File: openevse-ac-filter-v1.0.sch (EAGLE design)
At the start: 8 parts

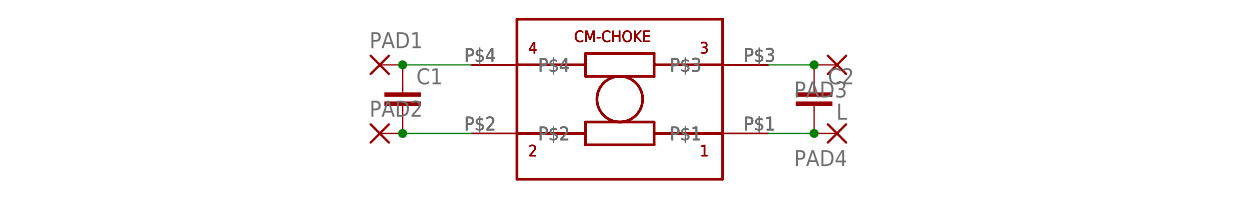
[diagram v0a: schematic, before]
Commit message: V1.2 increase pad and hole size
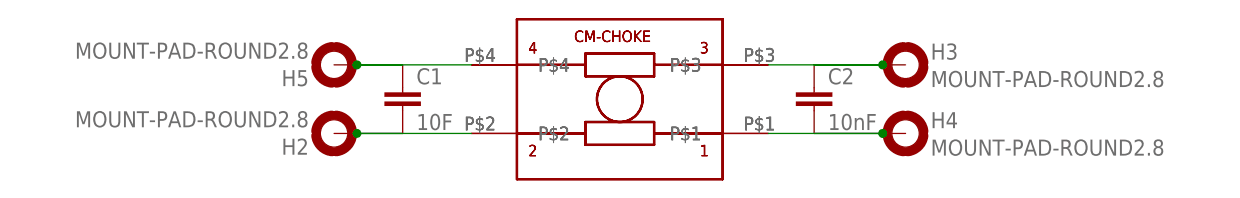
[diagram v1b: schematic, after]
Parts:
- removed PAD1, PAD2, PAD3: (no value), wirepad:2,54/0,9
- removed PAD4: L, wirepad:2,54/0,9
- added H2, H3, H4, H5: MOUNT-PAD-ROUND2.8, holes:MOUNT-PAD-ROUND2.8
- C1: value (none) -> 10F
- C2: value (none) -> 10nF
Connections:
- net N$1: now also H5.MOUNT; no longer PAD1.P
- net N$2: now also H2.MOUNT; no longer PAD2.P
- net N$3: now also H3.MOUNT; no longer PAD3.P
- net N$4: now also H4.MOUNT; no longer PAD4.P
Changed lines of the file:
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@@
 <?xml version="1.0" encoding="utf-8"?>
 <!DOCTYPE eagle SYSTEM "eagle.dtd">
-<eagle version="7.6.0">
+<eagle version="7.7.0">
 <drawing>
 <settings>
@@
 <part name="U$1" library="Schaffner-CM-Choke" deviceset="RN114-0.3-02-47M" device="" value="47mH"/>
 <part name="U$2" library="Schaffner-CM-Choke" deviceset="RN214-0.3-02-47M" device=""/>
-<part name="C1" library="capacitor-wima" deviceset="C" device="5/2.5"/>
-<part name="C2" library="capacitor-wima" deviceset="C" device="5/2.5"/>
-<part name="PAD1" library="wirepad" deviceset="2,54/0,9" device=""/>
-<part name="PAD2" library="wirepad" deviceset="2,54/0,9" device=""/>
-<part name="PAD3" library="wirepad" deviceset="2,54/0,9" device=""/>
-<part name="PAD4" library="wirepad" deviceset="2,54/0,9" device="" value="L"/>
+<part name="C1" library="capacitor-wima" deviceset="C" device="5/2.5" value="10F"/>
+<part name="C2" library="capacitor-wima" deviceset="C" device="5/2.5" value="10nF"/>
+<part name="H2" library="holes" deviceset="MOUNT-PAD-ROUND" device="2.8"/>
+<part name="H3" library="holes" deviceset="MOUNT-PAD-ROUND" device="2.8"/>
+<part name="H4" library="holes" deviceset="MOUNT-PAD-ROUND" device="2.8"/>
+<part name="H5" library="holes" deviceset="MOUNT-PAD-ROUND" device="2.8"/>
 </parts>
 <sheets>
@@
 <instance part="C1" gate="G$1" x="10.16" y="73.66"/>
 <instance part="C2" gate="G$1" x="55.88" y="73.66"/>
-<instance part="PAD1" gate="1" x="7.62" y="76.2"/>
-<instance part="PAD2" gate="1" x="7.62" y="68.58"/>
-<instance part="PAD3" gate="1" x="58.42" y="76.2" rot="R180"/>
-<instance part="PAD4" gate="1" x="58.42" y="68.58" rot="R180"/>
+<instance part="H2" gate="G$1" x="2.54" y="68.58" rot="R180"/>
+<instance part="H3" gate="G$1" x="66.04" y="76.2"/>
+<instance part="H4" gate="G$1" x="66.04" y="68.58"/>
+<instance part="H5" gate="G$1" x="2.54" y="76.2" rot="R180"/>
 </instances>
 <busses>
@@
 <pinref part="U$2" gate="G$1" pin="P$4"/>
 <pinref part="C1" gate="G$1" pin="1"/>
-<wire x1="17.78" y1="76.2" x2="10.16" y2="76.2" width="0.1524" layer="91"/>
-<pinref part="PAD1" gate="1" pin="P"/>
-<junction x="10.16" y="76.2"/>
+<wire x1="17.78" y1="76.2" x2="5.08" y2="76.2" width="0.1524" layer="91"/>
+<pinref part="H5" gate="G$1" pin="MOUNT"/>
+<junction x="5.08" y="76.2"/>
+<wire x1="5.08" y1="76.2" x2="10.16" y2="76.2" width="0.1524" layer="91"/>
 </segment>
 </net>
@@
 <pinref part="U$2" gate="G$1" pin="P$2"/>
 <pinref part="C1" gate="G$1" pin="2"/>
-<wire x1="10.16" y1="68.58" x2="17.78" y2="68.58" width="0.1524" layer="91"/>
-<pinref part="PAD2" gate="1" pin="P"/>
-<junction x="10.16" y="68.58"/>
+<wire x1="5.08" y1="68.58" x2="17.78" y2="68.58" width="0.1524" layer="91"/>
+<pinref part="H2" gate="G$1" pin="MOUNT"/>
+<junction x="5.08" y="68.58"/>
+<wire x1="5.08" y1="68.58" x2="10.16" y2="68.58" width="0.1524" layer="91"/>
 </segment>
 </net>
@@
 <pinref part="U$2" gate="G$1" pin="P$3"/>
 <pinref part="C2" gate="G$1" pin="1"/>
-<wire x1="50.8" y1="76.2" x2="55.88" y2="76.2" width="0.1524" layer="91"/>
-<pinref part="PAD3" gate="1" pin="P"/>
-<junction x="55.88" y="76.2"/>
+<wire x1="50.8" y1="76.2" x2="63.5" y2="76.2" width="0.1524" layer="91"/>
+<pinref part="H3" gate="G$1" pin="MOUNT"/>
+<junction x="63.5" y="76.2"/>
+<wire x1="63.5" y1="76.2" x2="55.88" y2="76.2" width="0.1524" layer="91"/>
 </segment>
 </net>
@@
 <pinref part="U$2" gate="G$1" pin="P$1"/>
 <pinref part="C2" gate="G$1" pin="2"/>
-<wire x1="50.8" y1="68.58" x2="55.88" y2="68.58" width="0.1524" layer="91"/>
-<pinref part="PAD4" gate="1" pin="P"/>
-<junction x="55.88" y="68.58"/>
+<wire x1="50.8" y1="68.58" x2="63.5" y2="68.58" width="0.1524" layer="91"/>
+<pinref part="H4" gate="G$1" pin="MOUNT"/>
+<junction x="63.5" y="68.58"/>
+<wire x1="63.5" y1="68.58" x2="55.88" y2="68.58" width="0.1524" layer="91"/>
 </segment>
 </net>
